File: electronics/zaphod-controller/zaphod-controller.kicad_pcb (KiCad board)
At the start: 4 copper layers, 199.9 x 69.3 mm, 249 parts, among them P1 MOLEX_43160-0102, P11 MOLEX_MINIFIT_JR_2x4_WAY, P12 MOLEX_MINIFIT_JR_2x4_WAY, P13 MOLEX_MINIFIT_JR_2x4_WAY, P14 MOLEX_MINIFIT_JR_2x4_WAY, P15 MOLEX_NANOFIT_2x4_WAY, P16 MOLEX_NANOFIT_1x6_WAY, P17 MOLEX_NANOFIT_2x3_WAY, P18 CONN_01X02, P19 MOLEX_KK2.54_1x4_WAY_FAN, P2 MOLEX_MINIFIT_JR_2x2_WAY, P20 CONN_01X06, P21 MOLEX_NANOFIT_2x5_WAY, P3 MOLEX_MINIFIT_JR_2x2_WAY, P4 MOLEX_MINIFIT_JR_2x2_WAY, P5 MOLEX_MINIFIT_JR_2x2_WAY, Q1 Si7852DP, Q2 Si7852DP, Q3 2N7002P, Q4 NTR1P02T1G, Q5 BC847B, Q6 2N7002P, SW1 B3U-1000P_SPST-NO_SMD, SW2 B3U-1000P_SPST-NO_SMD, SW3 B3U-1000P_SPST-NO_SMD, U1 ISL85410FRZ, U10 ULN2003A, U11 ULN2003A, U12 ADUM5412, U2 LM5116, U3 ISL85410FRZ, U4 STM32F429VET6, U5 ADUM3160, U6 ACS711KEXLT_15AB, U7 ACS711KEXLT_15AB, U8 ACS711KEXLT_15AB, U9 ACS711KEXLT_15AB, X1 CSTCE8M00G55Z, X2 SWD_SMT_SOCKET, X3 ABS06-107-32.768KHZ

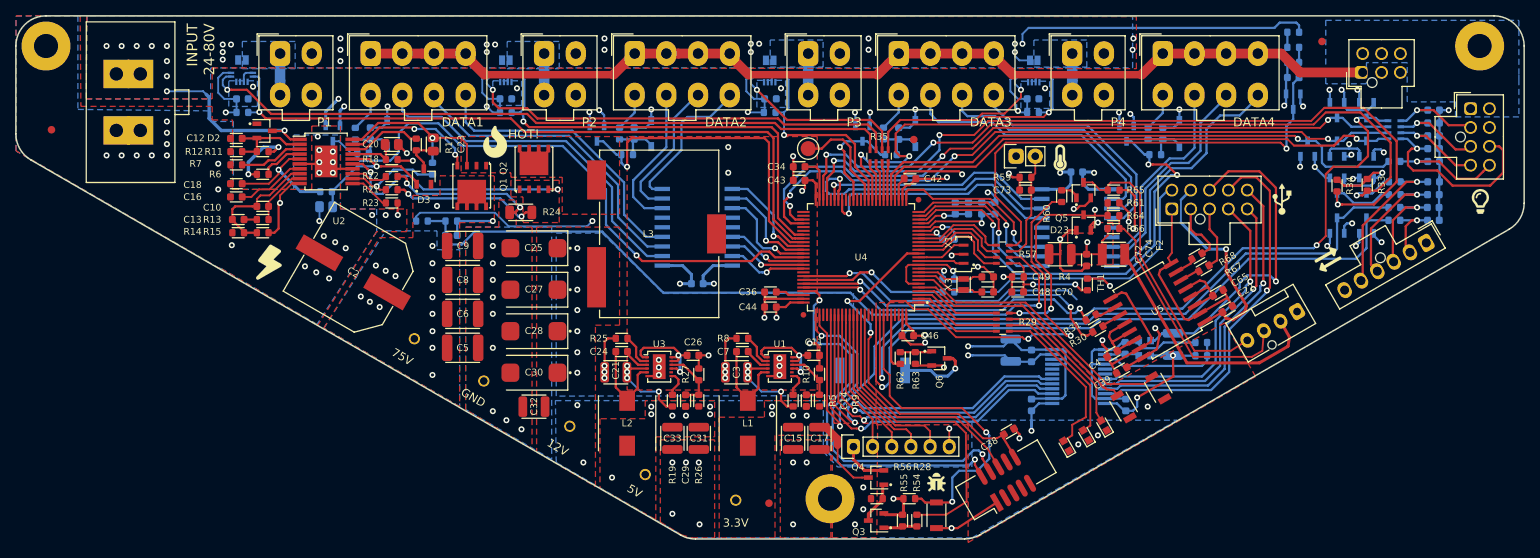
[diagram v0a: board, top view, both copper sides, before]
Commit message: PCB updates and minor tweaks
Based on review notes, few resistor changes, more stitching vias, increased clearances. Added polyfuse to add-in card module.
Tightened up soldermask clearances, etc.
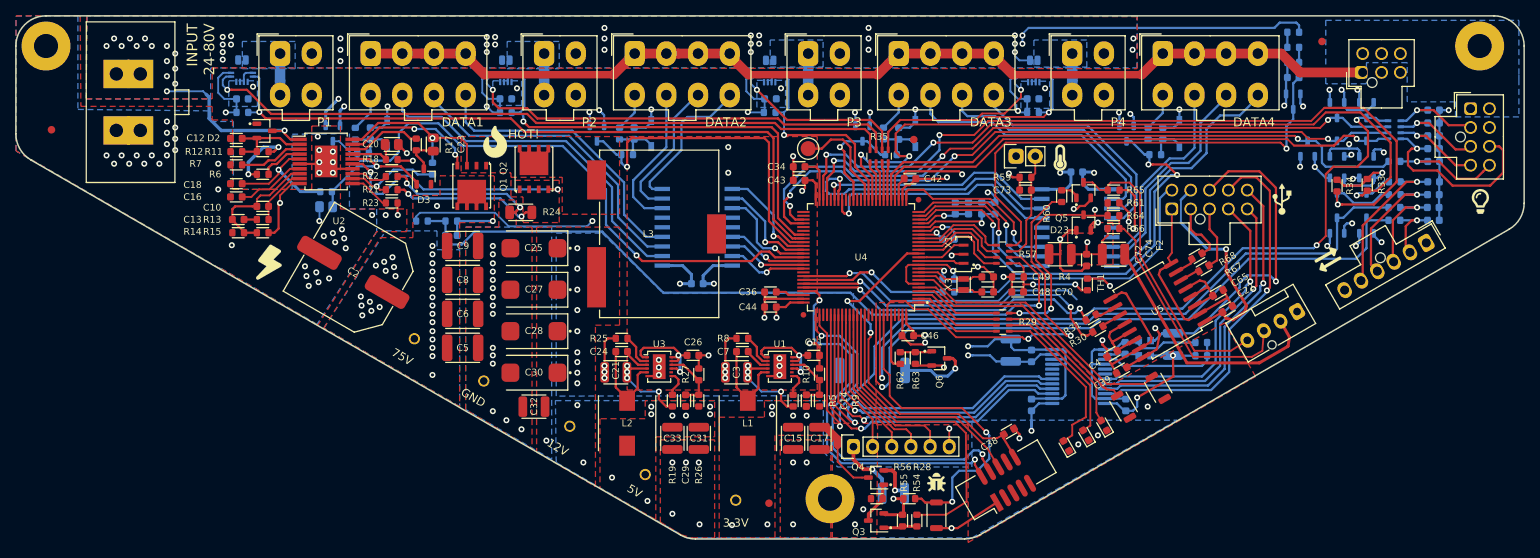
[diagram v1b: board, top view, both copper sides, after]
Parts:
- added F1: 0.5A_1210L_PTC, Applidyne_Fuse:FUSC3225X85L50N, B.Cu at (166.3, 113.3)
- R4, R58, R59: value 10K0_1608M -> 2K40_1608M
- R48: value 220R_QUAD_ARRAY_1608M -> 47R_QUAD_ARRAY_1608M
- R49: value 220R_1608M -> 10R_1608M
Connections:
- P20 pad 1: Net-(P20-Pad1) -> Net-(F1-Pad1)
- Q4 pad 2: Net-(P20-Pad1) -> Net-(F1-Pad2)
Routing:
- net Net-(F1-Pad1): track 0.00 -> 8.48 mm, vias 0 -> 1
- net Net-(P20-Pad1): track 6.33 -> 0.00 mm
- net Net-(F1-Pad2): track 0.00 -> 5.64 mm, vias 0 -> 1
- net +5V: track 165.4 -> 166.7 mm, vias 9 -> 10
- net GND: track 284.9 -> 285.4 mm, vias 112 -> 131
- net +3.3V: track 210.9 -> 210.8 mm, vias 36 -> 37
- net +POWER: vias 48 -> 77
- net +12V: vias 22 -> 25
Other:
- rule pad_to_mask_clearance: 0.2 -> 0.08

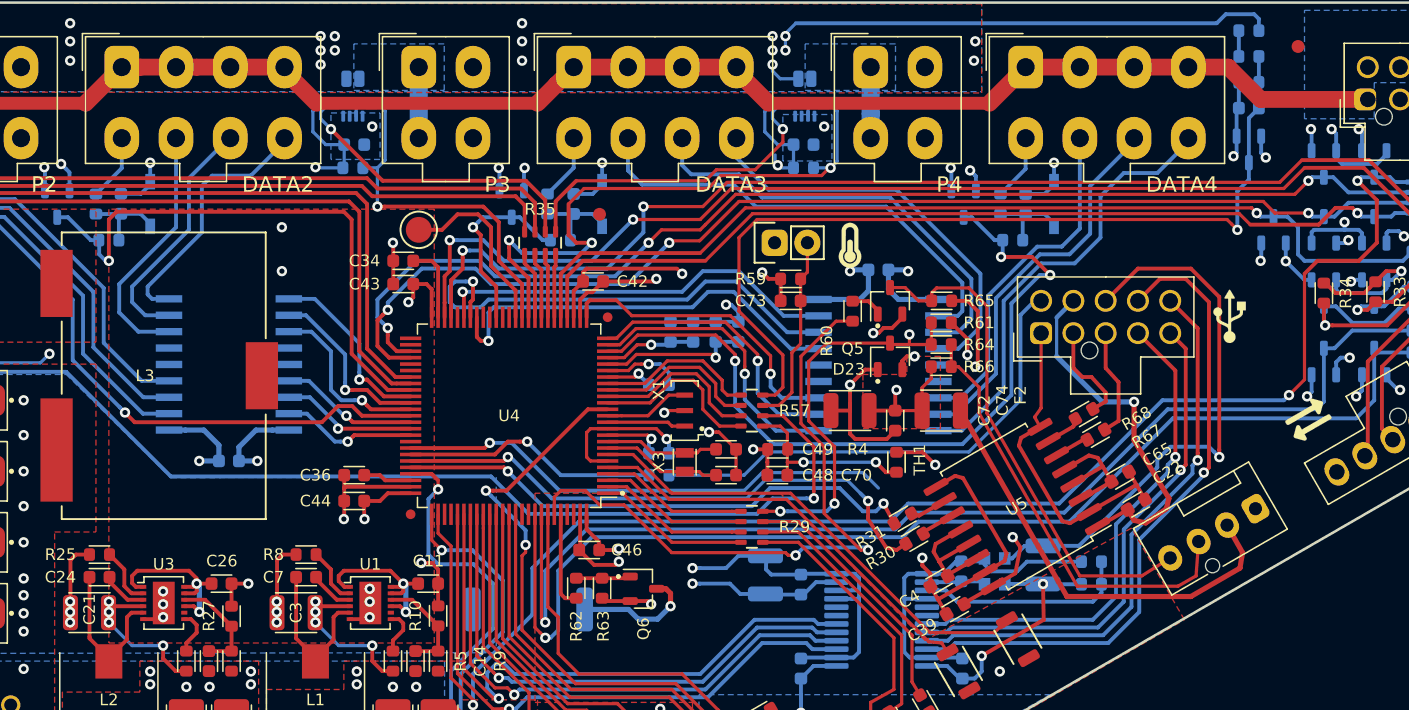
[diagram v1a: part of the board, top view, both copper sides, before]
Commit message: PCB power connector silkscreen note, VBUS on testpoint
The board is well and truly 'done' now.
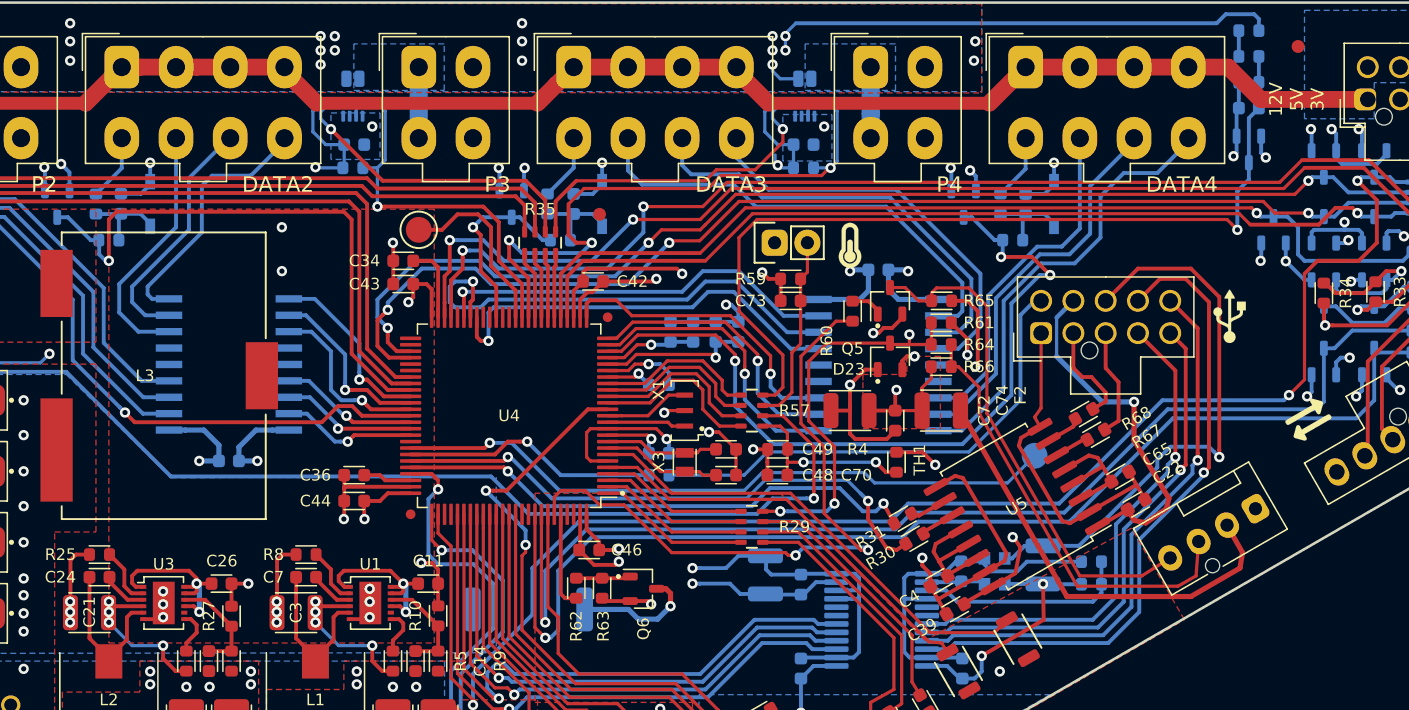
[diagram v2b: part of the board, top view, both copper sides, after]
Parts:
- added TEST6: PROBE_PAD, Applidyne_Test:TP200, B.Cu at (202.7, 85.1)
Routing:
- net USB_VBUS: track 39.0 -> 51.8 mm
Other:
- board text added: "12V 5V 3V"
- board text added: "VBUS"
